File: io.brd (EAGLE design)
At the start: 23 x 40 mm, 34 parts, among them J1 SJ-3523-SMT-TR, Q1 MMBT2222A-7-FSOT-23_DIO-M, Q2 2SCR574D3TL1TRANS_2SCR573_TO-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, U1 MCP1703T-5002E, U3 LM386M-1

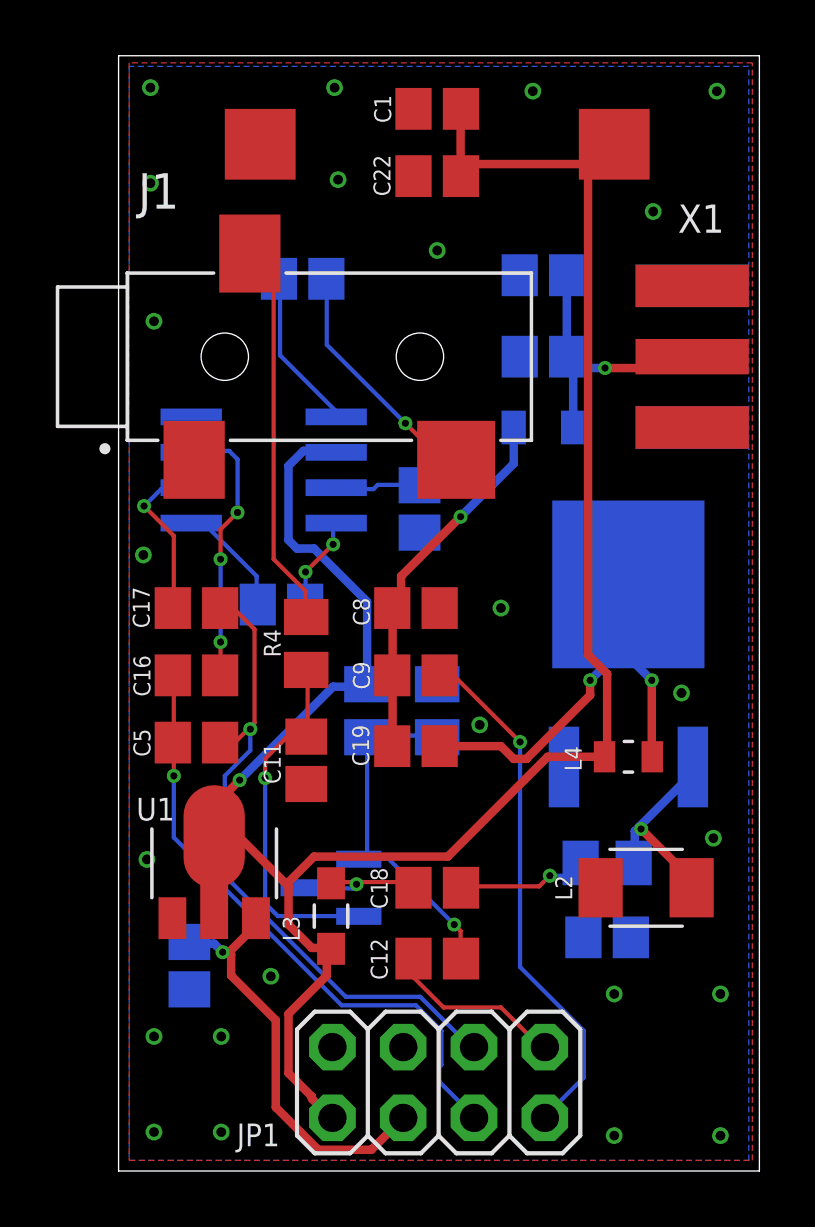
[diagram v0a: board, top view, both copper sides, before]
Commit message: v1.2 boards
* corrected C22 as a 33uF (vs 33pF) capacitor with a 1206 footprint
* Q2 emitter is now tied to Q1 emitter and KEY_IN to cut down on self resonance
* Unused pin 4 on JP1 now tied to GND
* All pins on JP1 labelled on top and bottom of each board
* lots more GND vias
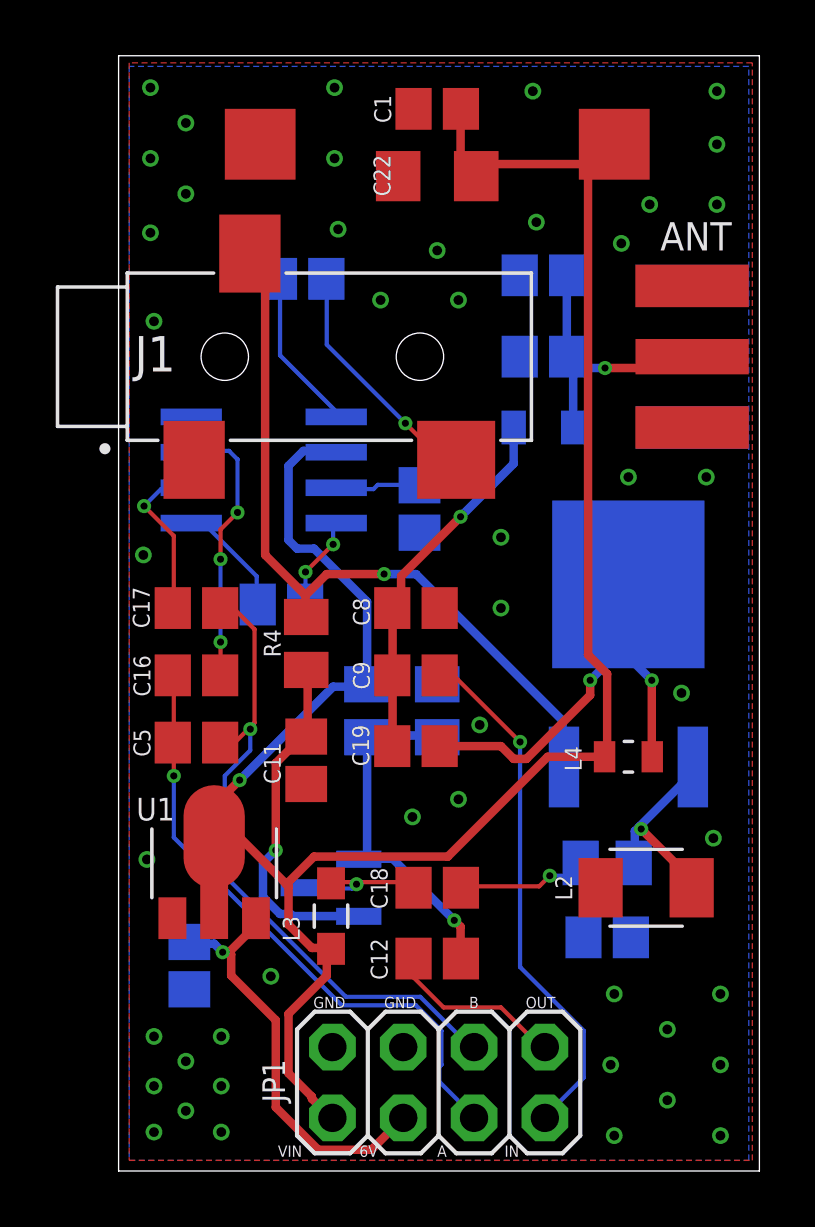
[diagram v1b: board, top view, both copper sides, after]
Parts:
- C22: device adafruit:C0805 -> adafruit:C1206
- renumbered X1 to ANT
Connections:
- net GND: now also JP1.4; no longer Q2.3
- net KEY_IN: now also Q2.3
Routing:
- net KEY_IN: track 13.9 -> 27.3 mm, vias 0 -> 1
- net VIN: track 79.9 -> 80.6 mm
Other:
- board text added: "6V"
- board text added: "9VμTX IO Board v1.2 K6GG & K6JCA"
- board text added: "A"
- board text added: "B"
- board text added: "GND"
- board text added: "IN"
- board text added: "OUT"
- board text added: "VIN"
- board text removed: "9VuTX IO Board v1.1a K6GG"

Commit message: v1.2 updated inductors
* updated L3 to a 650mA capable 5.6uH flat package
* updated L4 to a 3A capable 15uH flat package... 16uH are difficult to come by
* general board cleanup for readability
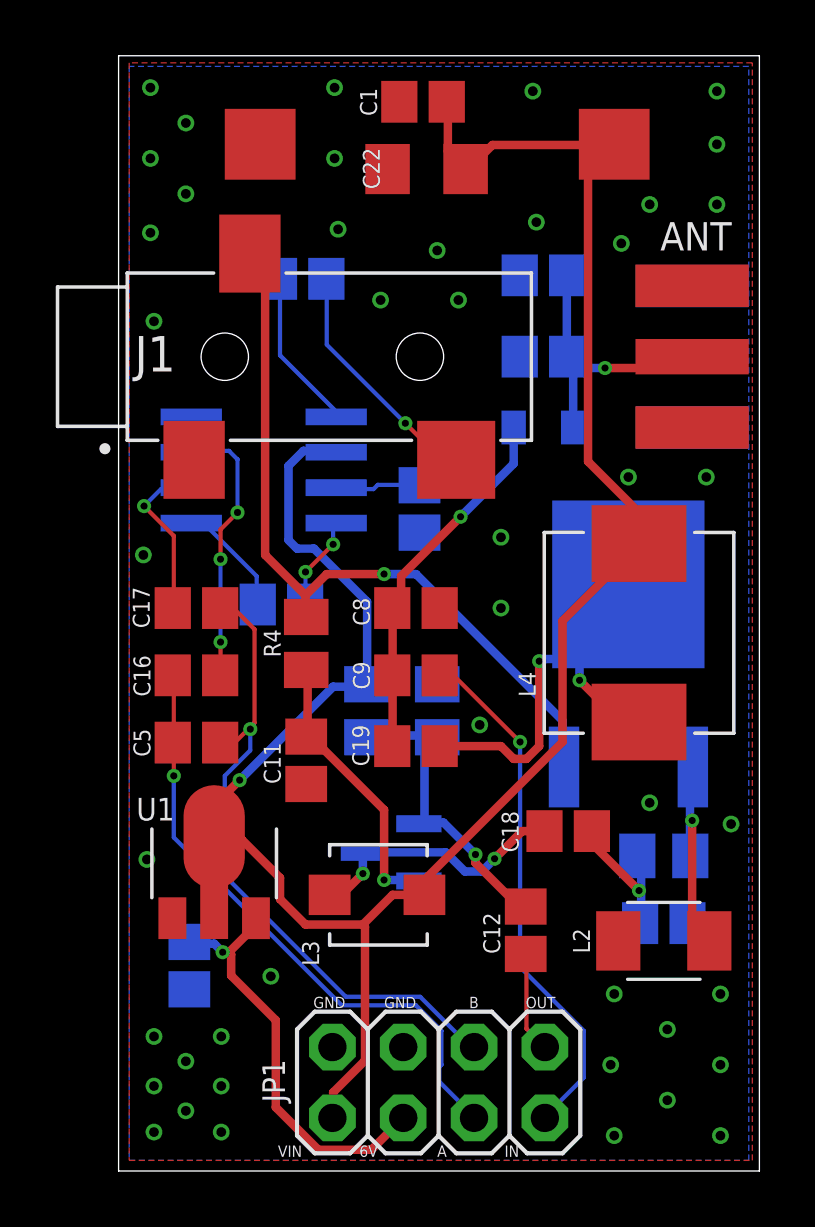
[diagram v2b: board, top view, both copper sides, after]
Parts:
- L3: device MLF2012E5R6KT000:INDC2012X87N -> zort2:SRP3012C
- L4: device LQW18AN16NG8ZD:INDC1609X100N -> zort2:ASPI-0630LR
- moved C18 5.12 mm to (16.1, 12.2)
- moved L4 4.46 mm to (18.7, 19.3), turned to 90 degrees
- moved C12 3.33 mm to (14.6, 8.64), turned to 90 degrees
- moved Q1 2.50 mm to (9.78, 11.4)
- moved C10 2.09 mm to (19.6, 8.89)
- moved R7 2.05 mm to (19.6, 11.3)
- moved L2 2.01 mm to (19.6, 8.26)
- moved L3 1.82 mm to (9.27, 9.91), turned to 0 degrees
- moved C1 0.57 mm to (10.9, 38.4)
- moved C22 0.46 mm to (11.0, 35.9)
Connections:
- net N$21: now also L3.P$1; no longer L3.1
- net N$24: now also L4.P$1; no longer L4.1
- net VIN: now also L3.P$2, L4.P$2; no longer L3.2, L4.2
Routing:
- net N$24: track 17.9 -> 24.9 mm
- net N$21: track 5.16 -> 9.67 mm, vias 1 -> 2
- net ANT_OUT: track 6.43 -> 3.63 mm
- net VIN: track 80.6 -> 78.1 mm
- net N$20: track 12.6 -> 10.2 mm
- net N$22: track 7.60 -> 5.42 mm
- net N$19: track 13.1 -> 12.0 mm

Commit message: Version 1.2 as ordered
* some slight cleanup in labels and routing after looking at the previews on oshpark
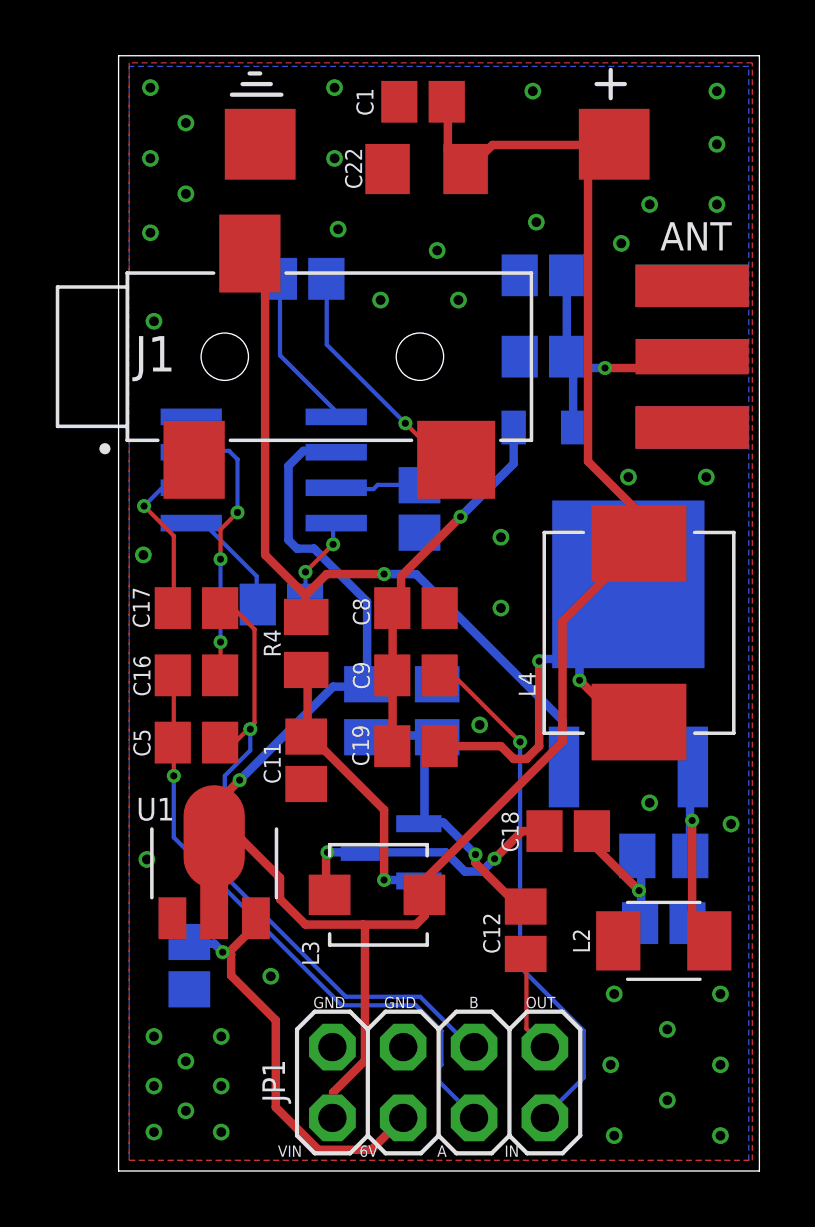
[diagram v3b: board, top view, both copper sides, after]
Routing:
- net N$21: track 9.67 -> 10.3 mm
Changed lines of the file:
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@@
 <text x="10.541" y="0.381" size="0.4064" layer="26" rot="MR0">6V</text>
 <text x="8.255" y="0.381" size="0.4064" layer="26" rot="MR0">VIN</text>
-<circle x="3.048" y="22.352" radius="0.254" width="0.1524" layer="22"/>
+<circle x="4.318" y="22.225" radius="0.254" width="0.1524" layer="22"/>
+<wire x1="3.302" y1="22.733" x2="7.112" y2="22.733" width="0.1524" layer="22"/>
+<wire x1="3.302" y1="27.559" x2="7.112" y2="27.559" width="0.1524" layer="22"/>
+<wire x1="4.445" y1="38.989" x2="5.461" y2="38.989" width="0.1524" layer="21"/>
+<wire x1="17.653" y1="39.497" x2="17.653" y2="38.481" width="0.1524" layer="21"/>
+<wire x1="17.145" y1="38.989" x2="18.161" y2="38.989" width="0.1524" layer="21"/>
+<wire x1="4.064" y1="38.608" x2="5.842" y2="38.608" width="0.1524" layer="21"/>
+<wire x1="4.699" y1="39.37" x2="5.08" y2="39.37" width="0.1524" layer="21"/>
 </plain>
 <attributes>
@@
 <elements>
 <element name="C1" library="adafruit" library_urn="urn:adsk.eagle:library:420" package="C0805" package3d_urn="urn:adsk.eagle:package:6240337/1" value="0.1U" x="10.922" y="38.354" smashed="yes" rot="R180">
-<attribute name="NAME" x="9.271" y="37.846" size="0.6096" layer="25" rot="R90"/>
+<attribute name="NAME" x="9.144" y="37.846" size="0.6096" layer="25" rot="R90"/>
 <attribute name="VALUE" x="12.573" y="38.862" size="0.3048" layer="27" rot="R270"/>
 </element>
@@
 </element>
 <element name="C22" library="adafruit" library_urn="urn:adsk.eagle:library:420" package="C1206" package3d_urn="urn:adsk.eagle:package:6240335/1" value="33U" x="11.049" y="35.941" smashed="yes" rot="R180">
-<attribute name="NAME" x="8.763" y="36.703" size="0.6096" layer="25" rot="R270"/>
+<attribute name="NAME" x="8.128" y="36.703" size="0.6096" layer="25" rot="R270"/>
 <attribute name="VALUE" x="12.7" y="36.322" size="0.3048" layer="27" rot="R270"/>
 </element>
@@
 <wire x1="3.8862" y1="12.0396" x2="3.429" y2="11.989" width="0.3048" layer="1"/>
 <via x="4.3434" y="14.0208" extent="1-16" drill="0.254"/>
-<wire x1="9.8298" y1="9.906" x2="10.971" y2="9.906" width="0.3048" layer="1"/>
-<wire x1="8.763" y1="8.8392" x2="9.8298" y2="9.906" width="0.3048" layer="1"/>
+<wire x1="10.971" y1="9.906" x2="10.971" y2="9.1422" width="0.3048" layer="1"/>
+<wire x1="10.971" y1="9.1422" x2="10.668" y2="8.8392" width="0.3048" layer="1"/>
 <wire x1="6.7056" y1="8.8392" x2="8.763" y2="8.8392" width="0.3048" layer="1"/>
+<wire x1="8.763" y1="8.8392" x2="10.668" y2="8.8392" width="0.3048" layer="1"/>
 <wire x1="5.7912" y1="9.7536" x2="6.7056" y2="8.8392" width="0.3048" layer="1"/>
 <wire x1="5.7912" y1="10.5156" x2="5.7912" y2="9.7536" width="0.3048" layer="1"/>
@@
 <contactref element="C18" pad="1"/>
 <contactref element="Q1" pad="3"/>
-<wire x1="8.001" y1="9.906" x2="7.571" y2="9.906" width="0.3048" layer="1"/>
-<wire x1="8.763" y1="10.668" x2="8.001" y2="9.906" width="0.3048" layer="1"/>
-<wire x1="8.763" y1="11.43" x2="8.763" y2="10.668" width="0.3048" layer="16"/>
-<wire x1="8.763" y1="11.43" x2="8.7832" y2="11.43" width="0.3048" layer="16"/>
+<wire x1="7.493" y1="11.43" x2="7.444" y2="11.381" width="0.3048" layer="1"/>
+<wire x1="7.444" y1="11.381" x2="7.444" y2="10.033" width="0.3048" layer="1"/>
+<wire x1="7.571" y1="9.906" x2="7.444" y2="10.033" width="0.3048" layer="1"/>
+<wire x1="7.493" y1="11.43" x2="8.7832" y2="11.43" width="0.3048" layer="16"/>
 <wire x1="14.478" y1="12.192" x2="15.279" y2="12.192" width="0.3048" layer="1"/>
 <wire x1="13.4874" y1="11.2014" x2="14.478" y2="12.192" width="0.3048" layer="1"/>
@@
 <wire x1="11.7348" y1="11.43" x2="12.4206" y2="10.7442" width="0.3048" layer="16"/>
 <wire x1="8.7832" y1="11.43" x2="11.7348" y2="11.43" width="0.3048" layer="16"/>
-<via x="8.763" y="10.668" extent="1-16" drill="0.254"/>
+<via x="7.493" y="11.43" extent="1-16" drill="0.254"/>
 <via x="13.4874" y="11.2014" extent="1-16" drill="0.254"/>
 </signal>

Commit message: v1.3
* replaced L5 and C19 with larger devices capable of more current
* replaced Q2 with another 2222A
* increased power and output wire size to 15mil (from 12)

Revisions based on testing with my amplifier circuit breakout
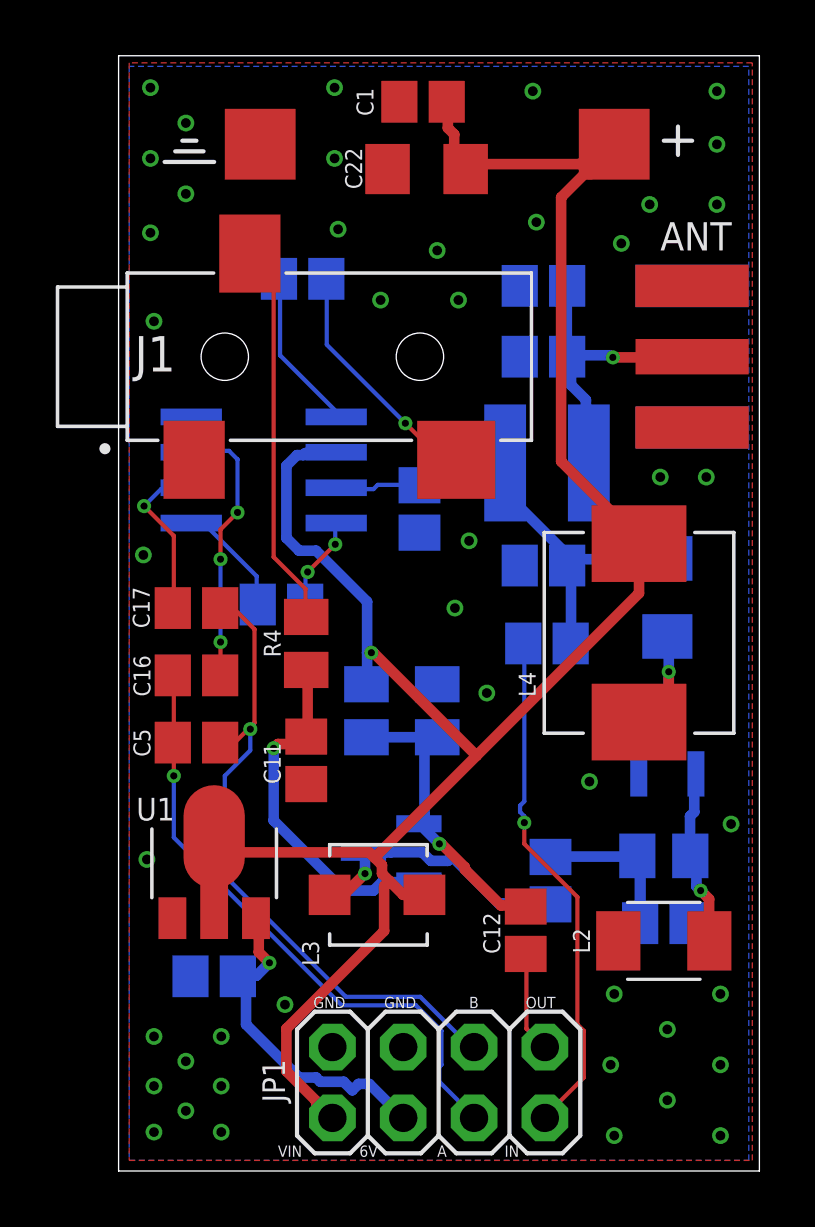
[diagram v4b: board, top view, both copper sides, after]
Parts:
- C19: device adafruit:C0805 -> adafruit:C1206
- L5: device Inductor:INDC2009X120 -> zort2:SRN4018TA
- Q2: value 2SCR574D3TL1TRANS_2SCR573_TO-252 -> MMBT2222A-7-FSOT-23_DIO-M; device zort2:TO-252 -> zort2:SOT-23_DIO-M
- moved C19 10.5 mm to (19.7, 20.6), flipped to the bottom, turned to 90 degrees
- moved C9 4.84 mm to (15.4, 18.9), flipped to the bottom
- moved C8 4.82 mm to (15.2, 21.7), flipped to the bottom
- moved Q2 3.35 mm to (19.7, 15.2)
- moved C18 1.89 mm to (15.5, 10.4), flipped to the bottom, turned to 90 degrees
- moved L5 1.28 mm to (15.4, 25.4)
- moved C2 0.97 mm to (3.43, 6.99), turned to 0 degrees
- moved C6 0.38 mm to (15.2, 31.8)
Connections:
- new net N$29: Q2.2
- net KEY_IN: no longer Q2.3
- net N$24: now also Q2.3; no longer Q2.2
- net N$25: now also L5.P$1; no longer L5.1
- net N$26: now also L5.P$2; no longer L5.2
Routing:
- net N$24: track 24.9 -> 5.22 mm, vias 2 -> 1
- net KEY_IN: track 27.3 -> 13.9 mm, vias 1 -> 0
- net N$22: track 5.42 -> 7.99 mm, vias 1 -> 0
- net N$20: track 10.2 -> 12.8 mm
- net N$23: track 8.90 -> 6.36 mm
- net 6V_DC: track 15.1 -> 12.6 mm
- net N$25: track 13.3 -> 11.2 mm, vias 1 -> 0
- net VIN: track 78.6 -> 77.6 mm
- net N$19: track 12.0 -> 11.3 mm
- net N$21: track 10.3 -> 10.2 mm, vias 2 -> 1
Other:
- board text added: "9VμTX I/O Board v1.3 K6GG & K6JCA"
- board text removed: "9VμTX IO Board v1.2 K6GG & K6JCA"
